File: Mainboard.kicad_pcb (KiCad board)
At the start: 4 copper layers, 100 x 60 mm, 137 parts, among them J1 USB_B_Micro, J10 Conn_01x02_Male, J11 Conn_01x02_Male, J12 Conn_01x02_Male, J2 8P8C_LED, J3 Micro_SD_Card_Det, J4 Conn_Coaxial, J5 Conn_Coaxial, J6 Screw_Terminal_01x02, J7 Screw_Terminal_01x02, J8 Screw_Terminal_01x02, J9 Conn_01x02_Male, Q1 MMDT2222A, Q3 PMV20ENR, Q4 PMV20ENR, Q5 PMV20ENR, U1 CP2102N-A01-GQFN24, U10 LTV-817S, U11 RFM95W-868S2, U2 SN65HVD230, U3 ESP32-WROOM-32D, U4 W25Q64FV, U5 MS5607-02BA, U6 MAX-M8Q, U7 LSM9DS1, U8 TPS63031, U9 LTV-817S

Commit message: routed almost all 3.3
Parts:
- removed REF** (x4): MountingHole_3.2mm_M3_DIN965_Pad, MountingHole:MountingHole_3.2mm_M3_DIN965_Pad
- added H1: MountingHole_Pad, MountingHole:MountingHole_3.2mm_M3_DIN965_Pad, F.Cu at (88.1, 53.1)
- added H2: MountingHole_Pad, MountingHole:MountingHole_3.2mm_M3_DIN965_Pad, F.Cu at (88.0, 107.0)
- added H3: MountingHole_Pad, MountingHole:MountingHole_3.2mm_M3_DIN965_Pad, F.Cu at (181.9, 53.0)
- added H4: MountingHole_Pad, MountingHole:MountingHole_3.2mm_M3_DIN965_Pad, F.Cu at (182.0, 107.0)
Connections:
- U3 pad 39: (no net) -> GND
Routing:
- net +3V3: track 90.6 -> 134.3 mm, vias 0 -> 16
- net GND: track 25.1 -> 27.9 mm
- added copper zone on In1.Cu, net +3V3

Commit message: update
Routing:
- net +3V3: track 134.3 -> 156.0 mm, vias 16 -> 18
- net VDD: track 17.0 -> 24.8 mm
- net GND: track 27.9 -> 30.0 mm, vias 0 -> 9

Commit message: update
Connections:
- U3 pad 8: /CAN_RX -> /CAN_TX
- U3 pad 9: /CAN_TX -> /CAN_RX
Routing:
- net /CAN_RX: track 50.0 -> 73.8 mm
- net /CAN_TX: track 67.1 -> 44.3 mm
- net GND: track 30.0 -> 43.3 mm, vias 9 -> 11
- net /LORA_CS: track 85.0 -> 91.6 mm
- net /Nuke1: track 88.9 -> 82.2 mm
- net /BOOT: track 82.7 -> 76.6 mm
- net /LORA_RESET: track 89.2 -> 83.4 mm
- net /SCL: track 112.1 -> 108.7 mm
- net /Buzzer: track 82.0 -> 84.9 mm
- net /CAN_HIGH: track 28.5 -> 26.3 mm
- net /SDA: track 104.8 -> 103.0 mm
- net /DTR: track 37.9 -> 36.3 mm
- net /FLASH_CS: track 88.2 -> 89.7 mm
- net /RADIO_RX: track 38.3 -> 39.8 mm
- net /RADIO_TX: track 37.8 -> 39.2 mm
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- removed copper zone on In1.Cu, net +3V3

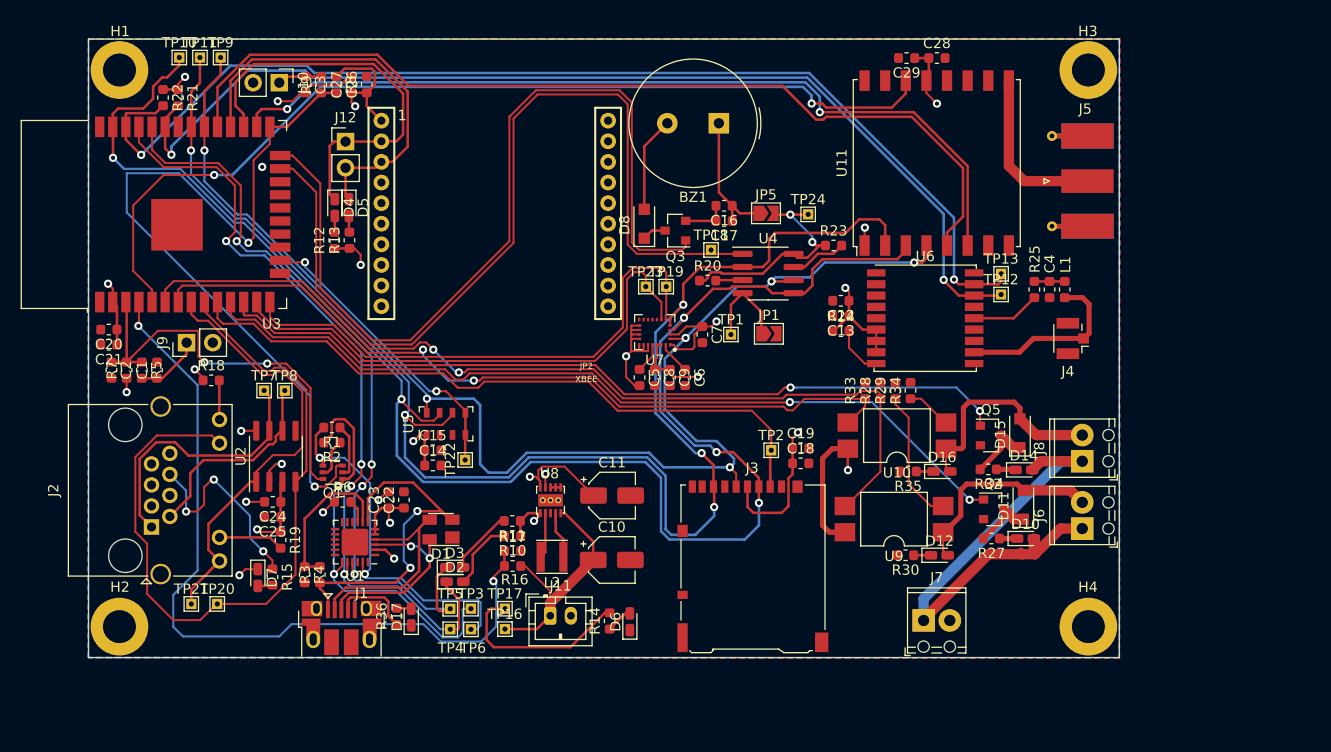
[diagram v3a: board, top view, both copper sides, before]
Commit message: replaced screw terminals with ramps connectors
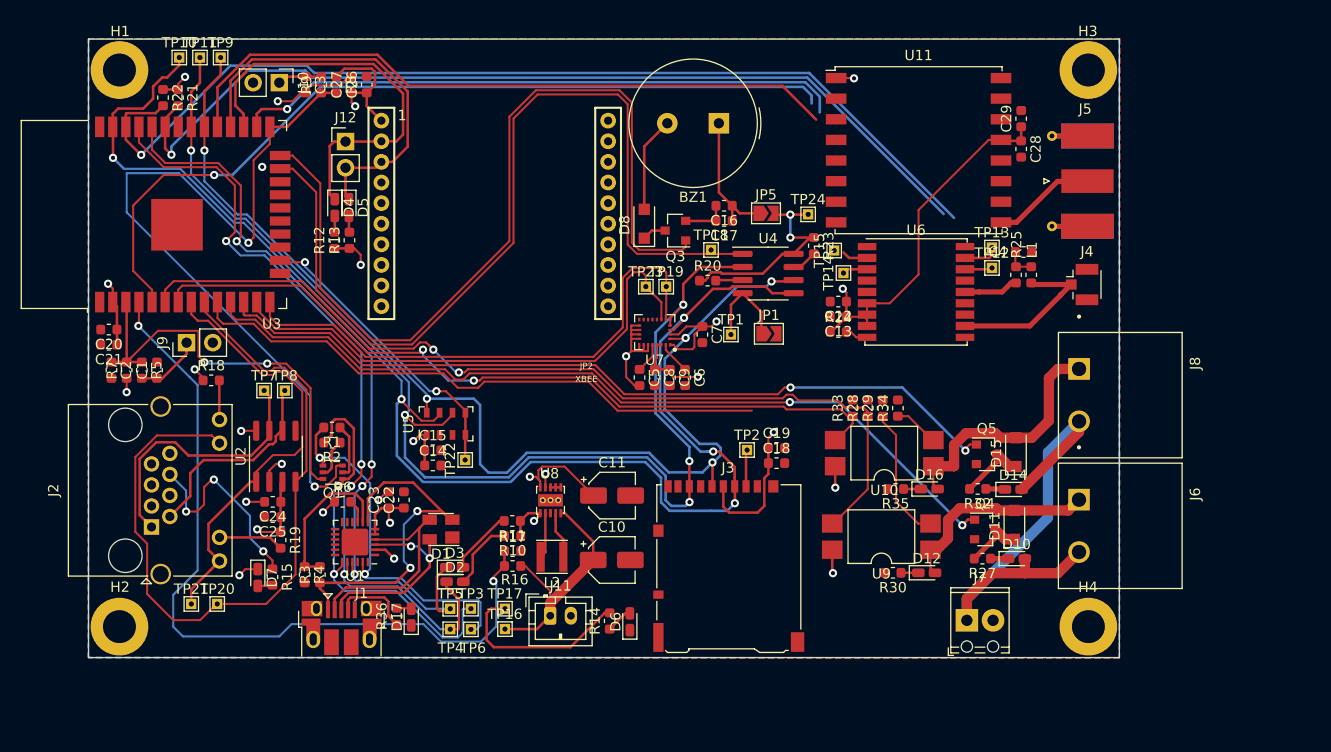
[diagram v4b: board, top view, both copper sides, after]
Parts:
- added TP14: TestPoint, TestPoint:TestPoint_THTPad_1.0x1.0mm_Drill0.5mm, F.Cu at (158.2, 72.7)
- added TP15: TestPoint, TestPoint:TestPoint_THTPad_1.0x1.0mm_Drill0.5mm, F.Cu at (157.3, 70.5)
- J6, J8: footprint TerminalBlock_Phoenix:TerminalBlock_Phoenix_MPT-0,5-2-2.54_1x02_P2.54mm_Horizontal -> iclr-hw:PHOENIX_1757242
- moved C29 12.6 mm to (175.5, 57.7), turned to 90 degrees
- moved C28 12.0 mm to (175.5, 60.7), turned to 270 degrees
- moved J8 7.40 mm to (185.1, 84.5), turned to 270 degrees
- moved J4 5.31 mm to (181.4, 73.8), turned to 0 degrees
- moved C4 4.43 mm to (175.7, 70.7), turned to 0 degrees
- moved J7 4.20 mm to (170.2, 106.4)
- moved J6 3.69 mm to (185.1, 97.2), turned to 270 degrees
- moved L1 3.55 mm to (176.5, 72.9)
- moved TP12 2.72 mm to (172.6, 72.2)
- moved TP13 2.70 mm to (172.6, 70.2)
- moved U6 2.70 mm to (165.3, 74.5)
- moved C18 2.34 mm to (151.7, 91.1)
- moved C19 2.34 mm to (151.7, 89.7)
- moved J3 2.34 mm to (147.1, 101.1)
- moved TP2 2.34 mm to (148.9, 89.9)
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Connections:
- J6 pad 1: /nukes/External_Supply -> Net-(D11-Pad2)
- J6 pad 2: Net-(D11-Pad2) -> /nukes/External_Supply
- J8 pad 1: /nukes/External_Supply -> Net-(D15-Pad2)
- J8 pad 2: Net-(D15-Pad2) -> /nukes/External_Supply
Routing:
- net /MISO: track 147.5 -> 119.8 mm
- net /LORA_CS: track 91.6 -> 67.1 mm
- net /LORA_RESET: track 83.4 -> 59.2 mm, vias 2 -> 1
- net /MOSI: track 162.3 -> 139.5 mm
- net /SCLK: track 132.9 -> 113.9 mm, vias 6 -> 5
- net /LORA_INT: track 93.5 -> 82.3 mm, vias 2 -> 1
- net +3V3: track 156.0 -> 166.7 mm
- net /SDA: track 103.0 -> 93.0 mm, vias 2 -> 1
- net /SCL: track 108.7 -> 100.6 mm, vias 2 -> 1
- net Net-(J5-Pad1): track 16.5 -> 10.0 mm
- net /SD_CS: track 69.8 -> 65.2 mm
- net Net-(R23-Pad2): track 5.53 -> 2.49 mm
- net Net-(D15-Pad2): track 21.6 -> 24.4 mm
- net Net-(R24-Pad2): track 4.89 -> 2.24 mm
- net /GPS/TXD: track 0.00 -> 2.51 mm
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
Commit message: udpate
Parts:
- added REF**: VIA-0.6mm, iclr-hw:VIA-0.6mm, F.Cu at (183.5, 77.8)
- added REF**: VIA-0.6mm, iclr-hw:VIA-0.6mm, F.Cu at (167.7, 72.6)
- added REF**: VIA-0.6mm, iclr-hw:VIA-0.6mm, F.Cu at (162.5, 72.6)
- added REF**: VIA-0.6mm, iclr-hw:VIA-0.6mm, F.Cu at (157.2, 72.6)
- added REF**: VIA-0.6mm, iclr-hw:VIA-0.6mm, F.Cu at (183.5, 67.3)
- added REF**: VIA-0.6mm, iclr-hw:VIA-0.6mm, F.Cu at (178.2, 67.3)
- added REF**: VIA-0.6mm, iclr-hw:VIA-0.6mm, F.Cu at (173.0, 67.3)
- added REF**: VIA-0.6mm, iclr-hw:VIA-0.6mm, F.Cu at (167.7, 67.3)
- added REF**: VIA-0.6mm, iclr-hw:VIA-0.6mm, F.Cu at (162.5, 67.3)
- added REF**: VIA-0.6mm, iclr-hw:VIA-0.6mm, F.Cu at (157.2, 67.3)
- added REF**: VIA-0.6mm, iclr-hw:VIA-0.6mm, F.Cu at (183.5, 62.1)
- added REF**: VIA-0.6mm, iclr-hw:VIA-0.6mm, F.Cu at (178.2, 77.8)
- added REF**: VIA-0.6mm, iclr-hw:VIA-0.6mm, F.Cu at (178.2, 62.1)
- added REF**: VIA-0.6mm, iclr-hw:VIA-0.6mm, F.Cu at (173.0, 62.1)
- added REF**: VIA-0.6mm, iclr-hw:VIA-0.6mm, F.Cu at (167.7, 62.1)
- added REF**: VIA-0.6mm, iclr-hw:VIA-0.6mm, F.Cu at (162.5, 62.1)
- added REF**: VIA-0.6mm, iclr-hw:VIA-0.6mm, F.Cu at (157.2, 62.1)
- added REF**: VIA-0.6mm, iclr-hw:VIA-0.6mm, F.Cu at (183.5, 56.8)
- added REF**: VIA-0.6mm, iclr-hw:VIA-0.6mm, F.Cu at (178.2, 56.8)
- added REF**: VIA-0.6mm, iclr-hw:VIA-0.6mm, F.Cu at (173.0, 56.8)
- added REF**: VIA-0.6mm, iclr-hw:VIA-0.6mm, F.Cu at (167.7, 56.8)
- added REF**: VIA-0.6mm, iclr-hw:VIA-0.6mm, F.Cu at (162.5, 56.8)
- added REF**: VIA-0.6mm, iclr-hw:VIA-0.6mm, F.Cu at (173.0, 77.8)
- added REF**: VIA-0.6mm, iclr-hw:VIA-0.6mm, F.Cu at (157.2, 56.8)
- added REF**: VIA-0.6mm, iclr-hw:VIA-0.6mm, F.Cu at (178.2, 51.6)
- added REF**: VIA-0.6mm, iclr-hw:VIA-0.6mm, F.Cu at (173.0, 51.6)
- added REF**: VIA-0.6mm, iclr-hw:VIA-0.6mm, F.Cu at (167.7, 51.6)
- added REF**: VIA-0.6mm, iclr-hw:VIA-0.6mm, F.Cu at (162.5, 51.6)
- added REF**: VIA-0.6mm, iclr-hw:VIA-0.6mm, F.Cu at (157.2, 51.6)
- added REF**: VIA-0.6mm, iclr-hw:VIA-0.6mm, F.Cu at (167.7, 77.8)
- added REF**: VIA-0.6mm, iclr-hw:VIA-0.6mm, F.Cu at (162.5, 77.8)
- added REF**: VIA-0.6mm, iclr-hw:VIA-0.6mm, F.Cu at (157.2, 77.8)
- added REF**: VIA-0.6mm, iclr-hw:VIA-0.6mm, F.Cu at (183.5, 72.6)
- added REF**: VIA-0.6mm, iclr-hw:VIA-0.6mm, F.Cu at (178.2, 72.6)
- added REF**: VIA-0.6mm, iclr-hw:VIA-0.6mm, F.Cu at (173.0, 72.6)
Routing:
- net /LORA_INT: track 82.3 -> 107.1 mm, vias 1 -> 2
- net /MISO: track 119.8 -> 142.4 mm, vias 5 -> 7
- net /MOSI: track 139.5 -> 161.4 mm, vias 5 -> 7
- net /SCLK: track 113.9 -> 133.6 mm, vias 5 -> 6
- net /LORA_RESET: track 59.2 -> 75.0 mm, vias 1 -> 2
- net +3V3: track 166.7 -> 179.2 mm, vias 18 -> 17
- net /SDA: track 93.0 -> 104.3 mm, vias 1 -> 2
- net /SCL: track 100.6 -> 109.8 mm, vias 1 -> 2
- net /LORA_CS: track 67.1 -> 74.0 mm
- net GND: track 43.0 -> 41.3 mm, vias 11 -> 10
- added copper zone on In1.Cu, net +3V3
- added copper zone on In1.Cu, net GND

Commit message: shroom
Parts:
- removed the REF** at (183.5, 77.8)
- removed the REF** at (167.7, 72.6)
- removed the REF** at (162.5, 72.6)
- removed the REF** at (157.2, 72.6)
- removed the REF** at (183.5, 67.3)
- removed the REF** at (178.2, 67.3)
- removed the REF** at (173.0, 67.3)
- removed the REF** at (167.7, 67.3)
- removed the REF** at (162.5, 67.3)
- removed the REF** at (157.2, 67.3)
- removed the REF** at (183.5, 62.1)
- removed the REF** at (178.2, 77.8)
- removed the REF** at (178.2, 62.1)
- removed the REF** at (173.0, 62.1)
- removed the REF** at (167.7, 62.1)
- removed the REF** at (162.5, 62.1)
- removed the REF** at (157.2, 62.1)
- removed the REF** at (183.5, 56.8)
- removed the REF** at (178.2, 56.8)
- removed the REF** at (173.0, 56.8)
- removed the REF** at (167.7, 56.8)
- removed the REF** at (162.5, 56.8)
- removed the REF** at (173.0, 77.8)
- removed the REF** at (157.2, 56.8)
- removed the REF** at (178.2, 51.6)
- removed the REF** at (173.0, 51.6)
- removed the REF** at (167.7, 51.6)
- removed the REF** at (162.5, 51.6)
- removed the REF** at (157.2, 51.6)
- removed the REF** at (167.7, 77.8)
- removed the REF** at (162.5, 77.8)
- removed the REF** at (157.2, 77.8)
- removed the REF** at (183.5, 72.6)
- removed the REF** at (178.2, 72.6)
- removed the REF** at (173.0, 72.6)
- added REF**: SolderJumper-3_P1.3mm_Bridged2Bar12_RoundedPad1.0x1.5mm_Num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, Jumper:SolderJumper-3_P1.3mm_Bridged2Bar12_RoundedPad1.0x1.5mm_NumberLabels, F.Cu at (102.9, 81.8)
- added REF**: VIA-0.6mm, iclr-hw:VIA-0.6mm, F.Cu at (176.8, 66.5)
- added REF**: VIA-0.6mm, iclr-hw:VIA-0.6mm, F.Cu at (176.1, 67.2)
- added REF**: VIA-0.6mm, iclr-hw:VIA-0.6mm, F.Cu at (175.4, 67.9)
- added REF**: VIA-0.6mm, iclr-hw:VIA-0.6mm, F.Cu at (174.6, 68.5)
- added REF**: VIA-0.6mm, iclr-hw:VIA-0.6mm, F.Cu at (177.7, 70.1)
- added REF**: VIA-0.6mm, iclr-hw:VIA-0.6mm, F.Cu at (177.7, 72.1)
- added REF**: VIA-0.6mm, iclr-hw:VIA-0.6mm, F.Cu at (177.7, 71.1)
- added REF**: VIA-0.6mm, iclr-hw:VIA-0.6mm, F.Cu at (178.2, 69.7)
- added REF**: VIA-0.6mm, iclr-hw:VIA-0.6mm, F.Cu at (176.5, 68.3)
- added REF**: VIA-0.6mm, iclr-hw:VIA-0.6mm, F.Cu at (176.2, 69.7)
- added REF**: SolderJumper-3_P1.3mm_Bridged2Bar12_RoundedPad1.0x1.5mm_Num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, Jumper:SolderJumper-3_P1.3mm_Bridged2Bar12_RoundedPad1.0x1.5mm_NumberLabels, F.Cu at (100.4, 81.8)
- added REF**: VIA-0.6mm, iclr-hw:VIA-0.6mm, F.Cu at (175.2, 69.7)
- added REF**: VIA-0.6mm, iclr-hw:VIA-0.6mm, F.Cu at (174.2, 69.7)
- added REF**: VIA-0.6mm, iclr-hw:VIA-0.6mm, F.Cu at (174.0, 70.8)
- added REF**: VIA-0.6mm, iclr-hw:VIA-0.6mm, F.Cu at (174.0, 71.8)
- added REF**: VIA-0.6mm, iclr-hw:VIA-0.6mm, F.Cu at (174.0, 72.8)
- added REF**: VIA-0.6mm, iclr-hw:VIA-0.6mm, F.Cu at (173.8, 73.8)
- added REF**: VIA-0.6mm, iclr-hw:VIA-0.6mm, F.Cu at (172.8, 73.8)
- added REF**: VIA-0.6mm, iclr-hw:VIA-0.6mm, F.Cu at (171.8, 73.8)
- added REF**: VIA-0.6mm, iclr-hw:VIA-0.6mm, F.Cu at (175.6, 74.7)
- added REF**: VIA-0.6mm, iclr-hw:VIA-0.6mm, F.Cu at (174.8, 75.2)
- added REF**: VIA-0.6mm, iclr-hw:VIA-0.6mm, F.Cu at (177.9, 63.3)
- added REF**: VIA-0.6mm, iclr-hw:VIA-0.6mm, F.Cu at (173.8, 75.2)
- added REF**: VIA-0.6mm, iclr-hw:VIA-0.6mm, F.Cu at (172.8, 75.2)
- added REF**: VIA-0.6mm, iclr-hw:VIA-0.6mm, F.Cu at (171.8, 75.2)
- added REF**: VIA-0.6mm, iclr-hw:VIA-0.6mm, F.Cu at (176.6, 74.6)
- added REF**: VIA-0.6mm, iclr-hw:VIA-0.6mm, F.Cu at (178.6, 74.5)
- added REF**: VIA-0.6mm, iclr-hw:VIA-0.6mm, F.Cu at (177.6, 74.5)
- added REF**: VIA-0.6mm, iclr-hw:VIA-0.6mm, F.Cu at (177.4, 73.1)
- added REF**: VIA-0.6mm, iclr-hw:VIA-0.6mm, F.Cu at (179.4, 73.1)
- added REF**: VIA-0.6mm, iclr-hw:VIA-0.6mm, F.Cu at (180.3, 72.8)
- added REF**: VIA-0.6mm, iclr-hw:VIA-0.6mm, F.Cu at (177.9, 75.2)
- added REF**: VIA-0.6mm, iclr-hw:VIA-0.6mm, F.Cu at (177.2, 64.0)
- added REF**: VIA-0.6mm, iclr-hw:VIA-0.6mm, F.Cu at (177.2, 75.9)
- added REF**: VIA-0.6mm, iclr-hw:VIA-0.6mm, F.Cu at (176.5, 76.6)
- added REF**: VIA-0.6mm, iclr-hw:VIA-0.6mm, F.Cu at (176.9, 76.8)
- added REF**: VIA-0.6mm, iclr-hw:VIA-0.6mm, F.Cu at (175.9, 76.8)
- added REF**: VIA-0.6mm, iclr-hw:VIA-0.6mm, F.Cu at (174.9, 76.8)
- added REF**: VIA-0.6mm, iclr-hw:VIA-0.6mm, F.Cu at (173.9, 76.8)
- added REF**: VIA-0.6mm, iclr-hw:VIA-0.6mm, F.Cu at (172.9, 76.8)
- added REF**: VIA-0.6mm, iclr-hw:VIA-0.6mm, F.Cu at (176.9, 78.3)
- added REF**: VIA-0.6mm, iclr-hw:VIA-0.6mm, F.Cu at (175.9, 78.3)
- added REF**: VIA-0.6mm, iclr-hw:VIA-0.6mm, F.Cu at (180.2, 74.9)
- added REF**: VIA-0.6mm, iclr-hw:VIA-0.6mm, F.Cu at (176.5, 64.7)
- added REF**: VIA-0.6mm, iclr-hw:VIA-0.6mm, F.Cu at (179.2, 76.0)
- added REF**: VIA-0.6mm, iclr-hw:VIA-0.6mm, F.Cu at (178.8, 76.3)
- added REF**: VIA-0.6mm, iclr-hw:VIA-0.6mm, F.Cu at (178.1, 77.1)
- added REF**: VIA-0.6mm, iclr-hw:VIA-0.6mm, F.Cu at (177.9, 78.3)
- added REF**: VIA-0.6mm, iclr-hw:VIA-0.6mm, F.Cu at (174.9, 78.3)
- added REF**: VIA-0.6mm, iclr-hw:VIA-0.6mm, F.Cu at (173.9, 78.3)
- added REF**: VIA-0.6mm, iclr-hw:VIA-0.6mm, F.Cu at (183.5, 78.3)
- added REF**: VIA-0.6mm, iclr-hw:VIA-0.6mm, F.Cu at (177.4, 77.8)
- added REF**: VIA-0.6mm, iclr-hw:VIA-0.6mm, F.Cu at (172.9, 78.3)
- added REF**: VIA-0.6mm, iclr-hw:VIA-0.6mm, F.Cu at (167.6, 78.3)
- added REF**: VIA-0.6mm, iclr-hw:VIA-0.6mm, F.Cu at (175.8, 65.4)
- added REF**: VIA-0.6mm, iclr-hw:VIA-0.6mm, F.Cu at (162.3, 78.3)
- added REF**: VIA-0.6mm, iclr-hw:VIA-0.6mm, F.Cu at (183.5, 73.0)
- added REF**: VIA-0.6mm, iclr-hw:VIA-0.6mm, F.Cu at (178.4, 73.1)
- added REF**: VIA-0.6mm, iclr-hw:VIA-0.6mm, F.Cu at (167.6, 73.0)
- added REF**: VIA-0.6mm, iclr-hw:VIA-0.6mm, F.Cu at (162.3, 73.0)
- added REF**: VIA-0.6mm, iclr-hw:VIA-0.6mm, F.Cu at (157.0, 73.0)
- added REF**: VIA-0.6mm, iclr-hw:VIA-0.6mm, F.Cu at (183.5, 67.7)
- added REF**: VIA-0.6mm, iclr-hw:VIA-0.6mm, F.Cu at (178.2, 67.7)
- added REF**: VIA-0.6mm, iclr-hw:VIA-0.6mm, F.Cu at (172.9, 67.7)
- added REF**: VIA-0.6mm, iclr-hw:VIA-0.6mm, F.Cu at (167.6, 67.7)
- added REF**: VIA-0.6mm, iclr-hw:VIA-0.6mm, F.Cu at (175.1, 66.1)
- added REF**: VIA-0.6mm, iclr-hw:VIA-0.6mm, F.Cu at (162.3, 67.7)
- added REF**: VIA-0.6mm, iclr-hw:VIA-0.6mm, F.Cu at (157.0, 67.7)
- added REF**: VIA-0.6mm, iclr-hw:VIA-0.6mm, F.Cu at (183.5, 62.4)
- added REF**: VIA-0.6mm, iclr-hw:VIA-0.6mm, F.Cu at (178.2, 62.4)
- added REF**: VIA-0.6mm, iclr-hw:VIA-0.6mm, F.Cu at (172.9, 62.4)
- added REF**: VIA-0.6mm, iclr-hw:VIA-0.6mm, F.Cu at (167.6, 62.4)
- added REF**: VIA-0.6mm, iclr-hw:VIA-0.6mm, F.Cu at (162.3, 62.4)
- added REF**: VIA-0.6mm, iclr-hw:VIA-0.6mm, F.Cu at (157.0, 62.4)
- added REF**: VIA-0.6mm, iclr-hw:VIA-0.6mm, F.Cu at (183.5, 57.1)
- added REF**: VIA-0.6mm, iclr-hw:VIA-0.6mm, F.Cu at (178.2, 57.1)
- added REF**: VIA-0.6mm, iclr-hw:VIA-0.6mm, F.Cu at (174.4, 66.8)
- added REF**: VIA-0.6mm, iclr-hw:VIA-0.6mm, F.Cu at (172.9, 57.1)
- added REF**: VIA-0.6mm, iclr-hw:VIA-0.6mm, F.Cu at (167.6, 57.1)
- added REF**: VIA-0.6mm, iclr-hw:VIA-0.6mm, F.Cu at (162.3, 57.1)
- added REF**: VIA-0.6mm, iclr-hw:VIA-0.6mm, F.Cu at (157.0, 57.1)
- added REF**: VIA-0.6mm, iclr-hw:VIA-0.6mm, F.Cu at (178.2, 51.8)
- added REF**: VIA-0.6mm, iclr-hw:VIA-0.6mm, F.Cu at (172.9, 51.8)
- added REF**: VIA-0.6mm, iclr-hw:VIA-0.6mm, F.Cu at (167.6, 51.8)
- added REF**: VIA-0.6mm, iclr-hw:VIA-0.6mm, F.Cu at (162.3, 51.8)
- added REF**: VIA-0.6mm, iclr-hw:VIA-0.6mm, F.Cu at (157.0, 51.8)
- added REF**: VIA-0.6mm, iclr-hw:VIA-0.6mm, F.Cu at (178.2, 65.0)
- J7: footprint TerminalBlock_Phoenix:TerminalBlock_Phoenix_MPT-0,5-2-2.54_1x02_P2.54mm_Horizontal -> iclr-hw:PHOENIX_1757242
- U1: footprint Package_DFN_QFN:QFN-24-1EP_4x4mm_P0.5mm_EP2.6x2.6mm -> Package_DFN_QFN:QFN-24-1EP_4x4mm_P0.5mm_EP2.6x2.6mm_ThermalVias
- moved J7 3.16 mm to (168.1, 108.8), turned to 180 degrees
- moved D10 2.99 mm to (175.2, 97.4)
- moved D11 2.99 mm to (175.0, 94.1)
- moved D16 2.99 mm to (166.7, 90.7)
- moved Q5 2.99 mm to (172.3, 87.3)
- moved R28 2.99 mm to (160.8, 82.8)
- moved R30 2.99 mm to (163.2, 98.8)
- moved R33 2.99 mm to (159.3, 82.8)
- moved U10 2.99 mm to (162.4, 87.2)
- moved D12 2.99 mm to (166.5, 98.8)
- moved Q4 2.99 mm to (172.1, 94.6)
- moved R27 2.99 mm to (171.9, 97.4)
- moved R34 2.99 mm to (163.7, 82.8)
- moved R35 2.99 mm to (163.5, 90.7)
- moved U9 2.99 mm to (162.1, 95.3)
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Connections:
- J7 pad 1: /nukes/External_Supply -> GND
- J7 pad 2: GND -> /nukes/External_Supply
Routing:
- net /EN: track 41.2 -> 48.0 mm
- net /CAN_LOW: track 19.9 -> 26.0 mm, vias 0 -> 1
- net /CAN_HIGH: track 26.3 -> 32.4 mm
- net GND: track 41.3 -> 46.1 mm
- net /BOOT: track 76.6 -> 81.3 mm
- net /nukes/External_Supply: track 49.0 -> 53.0 mm
- net +3V3: track 179.2 -> 183.1 mm, vias 17 -> 15
- net Net-(D15-Pad2): track 24.4 -> 20.6 mm
- net /CAN_TX: track 44.3 -> 47.0 mm
- net /TXD: track 75.5 -> 77.5 mm
- net /CAN_RX: track 73.8 -> 75.6 mm
- net /RXD: track 78.2 -> 79.7 mm
- net /Cont2: track 76.0 -> 77.3 mm
- net /SD_CS: track 65.2 -> 66.5 mm
- net /RTS: track 40.3 -> 41.6 mm
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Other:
- net class rf1 added: clearance 0.2, trace_width 0.33559, via_dia 0.8, via_drill 0.4

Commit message: stiched
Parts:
- added J3: Micro_SD_Card_Det, Connector_Card:microSD_HC_Hirose_DM3AT-SF-PEJM5, F.Cu at (147.1, 98.4)
- added REF**: VIA-0.6mm, iclr-hw:VIA-0.6mm, F.Cu at (184.5, 101.8)
- added REF**: VIA-0.6mm, iclr-hw:VIA-0.6mm, F.Cu at (184.5, 81.5)
- added REF**: VIA-0.6mm, iclr-hw:VIA-0.6mm, F.Cu at (85.5, 96.2)
- added REF**: VIA-0.6mm, iclr-hw:VIA-0.6mm, F.Cu at (85.5, 83.5)
- added REF**: VIA-0.6mm, iclr-hw:VIA-0.6mm, F.Cu at (85.5, 81.0)
- added REF**: VIA-0.6mm, iclr-hw:VIA-0.6mm, F.Cu at (85.5, 103.9)
- added REF**: VIA-0.6mm, iclr-hw:VIA-0.6mm, F.Cu at (85.5, 101.3)
- added REF**: VIA-0.6mm, iclr-hw:VIA-0.6mm, F.Cu at (85.5, 98.8)
- added REF**: VIA-0.6mm, iclr-hw:VIA-0.6mm, F.Cu at (85.5, 93.7)
- added REF**: VIA-0.6mm, iclr-hw:VIA-0.6mm, F.Cu at (85.5, 91.2)
- added REF**: VIA-0.6mm, iclr-hw:VIA-0.6mm, F.Cu at (85.5, 88.6)
- added REF**: VIA-0.6mm, iclr-hw:VIA-0.6mm, F.Cu at (184.5, 89.2)
- added REF**: VIA-0.6mm, iclr-hw:VIA-0.6mm, F.Cu at (85.5, 86.1)
- added REF**: VIA-0.6mm, iclr-hw:VIA-0.6mm, F.Cu at (85.5, 73.4)
- added REF**: VIA-0.6mm, iclr-hw:VIA-0.6mm, F.Cu at (85.5, 70.8)
- added REF**: VIA-0.6mm, iclr-hw:VIA-0.6mm, F.Cu at (85.5, 68.3)
- added REF**: VIA-0.6mm, iclr-hw:VIA-0.6mm, F.Cu at (85.5, 65.8)
- added REF**: VIA-0.6mm, iclr-hw:VIA-0.6mm, F.Cu at (85.5, 63.2)
- added REF**: VIA-0.6mm, iclr-hw:VIA-0.6mm, F.Cu at (85.5, 60.7)
- added REF**: VIA-0.6mm, iclr-hw:VIA-0.6mm, F.Cu at (85.5, 55.6)
- added REF**: VIA-0.6mm, iclr-hw:VIA-0.6mm, F.Cu at (131.2, 109.5)
- added REF**: VIA-0.6mm, iclr-hw:VIA-0.6mm, F.Cu at (118.5, 109.5)
- added REF**: VIA-0.6mm, iclr-hw:VIA-0.6mm, F.Cu at (184.5, 86.6)
- added REF**: VIA-0.6mm, iclr-hw:VIA-0.6mm, F.Cu at (116.0, 109.5)
- added REF**: VIA-0.6mm, iclr-hw:VIA-0.6mm, F.Cu at (113.5, 109.5)
- added REF**: VIA-0.6mm, iclr-hw:VIA-0.6mm, F.Cu at (177.0, 109.5)
- added REF**: VIA-0.6mm, iclr-hw:VIA-0.6mm, F.Cu at (174.4, 109.5)
- added REF**: VIA-0.6mm, iclr-hw:VIA-0.6mm, F.Cu at (171.9, 109.5)
- added REF**: VIA-0.6mm, iclr-hw:VIA-0.6mm, F.Cu at (169.3, 109.5)
- added REF**: VIA-0.6mm, iclr-hw:VIA-0.6mm, F.Cu at (166.8, 109.5)
- added REF**: VIA-0.6mm, iclr-hw:VIA-0.6mm, F.Cu at (164.3, 109.5)
- added REF**: VIA-0.6mm, iclr-hw:VIA-0.6mm, F.Cu at (161.7, 109.5)
- added REF**: VIA-0.6mm, iclr-hw:VIA-0.6mm, F.Cu at (159.2, 109.5)
- added REF**: VIA-0.6mm, iclr-hw:VIA-0.6mm, F.Cu at (184.5, 84.1)
- added REF**: VIA-0.6mm, iclr-hw:VIA-0.6mm, F.Cu at (156.7, 109.5)
- added REF**: VIA-0.6mm, iclr-hw:VIA-0.6mm, F.Cu at (151.6, 109.5)
- added REF**: VIA-0.6mm, iclr-hw:VIA-0.6mm, F.Cu at (149.0, 109.5)
- added REF**: VIA-0.6mm, iclr-hw:VIA-0.6mm, F.Cu at (146.5, 109.5)
- added REF**: VIA-0.6mm, iclr-hw:VIA-0.6mm, F.Cu at (143.9, 109.5)
- added REF**: VIA-0.6mm, iclr-hw:VIA-0.6mm, F.Cu at (141.4, 109.5)
- added REF**: VIA-0.6mm, iclr-hw:VIA-0.6mm, F.Cu at (138.9, 109.5)
- added REF**: VIA-0.6mm, iclr-hw:VIA-0.6mm, F.Cu at (136.3, 109.5)
- added REF**: VIA-0.6mm, iclr-hw:VIA-0.6mm, F.Cu at (133.8, 109.5)
- added REF**: VIA-0.6mm, iclr-hw:VIA-0.6mm, F.Cu at (128.7, 109.5)
- added REF**: VIA-0.6mm, iclr-hw:VIA-0.6mm, F.Cu at (184.5, 104.4)
- added REF**: VIA-0.6mm, iclr-hw:VIA-0.6mm, F.Cu at (126.2, 109.5)
- added REF**: VIA-0.6mm, iclr-hw:VIA-0.6mm, F.Cu at (123.6, 109.5)
- added REF**: VIA-0.6mm, iclr-hw:VIA-0.6mm, F.Cu at (121.1, 109.5)
- added REF**: VIA-0.6mm, iclr-hw:VIA-0.6mm, F.Cu at (110.9, 109.5)
- added REF**: VIA-0.6mm, iclr-hw:VIA-0.6mm, F.Cu at (108.4, 109.5)
- added REF**: VIA-0.6mm, iclr-hw:VIA-0.6mm, F.Cu at (105.8, 109.5)
- added REF**: VIA-0.6mm, iclr-hw:VIA-0.6mm, F.Cu at (103.3, 109.5)
- added REF**: VIA-0.6mm, iclr-hw:VIA-0.6mm, F.Cu at (100.8, 109.5)
- added REF**: VIA-0.6mm, iclr-hw:VIA-0.6mm, F.Cu at (98.2, 109.5)
- added REF**: VIA-0.6mm, iclr-hw:VIA-0.6mm, F.Cu at (95.7, 109.5)
- added REF**: VIA-0.6mm, iclr-hw:VIA-0.6mm, F.Cu at (184.5, 99.3)
- added REF**: VIA-0.6mm, iclr-hw:VIA-0.6mm, F.Cu at (93.2, 109.5)
- added REF**: VIA-0.6mm, iclr-hw:VIA-0.6mm, F.Cu at (91.0, 50.5)
- added REF**: VIA-0.6mm, iclr-hw:VIA-0.6mm, F.Cu at (136.8, 50.5)
- added REF**: VIA-0.6mm, iclr-hw:VIA-0.6mm, F.Cu at (124.1, 50.5)
- added REF**: VIA-0.6mm, iclr-hw:VIA-0.6mm, F.Cu at (121.5, 50.5)
- added REF**: VIA-0.6mm, iclr-hw:VIA-0.6mm, F.Cu at (119.0, 50.5)
- added REF**: VIA-0.6mm, iclr-hw:VIA-0.6mm, F.Cu at (154.6, 50.5)
- added REF**: VIA-0.6mm, iclr-hw:VIA-0.6mm, F.Cu at (152.0, 50.5)
- added REF**: VIA-0.6mm, iclr-hw:VIA-0.6mm, F.Cu at (149.5, 50.5)
- added REF**: VIA-0.6mm, iclr-hw:VIA-0.6mm, F.Cu at (146.9, 50.5)
- added REF**: VIA-0.6mm, iclr-hw:VIA-0.6mm, F.Cu at (184.5, 96.8)
- added REF**: VIA-0.6mm, iclr-hw:VIA-0.6mm, F.Cu at (144.4, 50.5)
- added REF**: VIA-0.6mm, iclr-hw:VIA-0.6mm, F.Cu at (141.8, 50.5)
- added REF**: VIA-0.6mm, iclr-hw:VIA-0.6mm, F.Cu at (139.3, 50.5)
- added REF**: VIA-0.6mm, iclr-hw:VIA-0.6mm, F.Cu at (134.2, 50.5)
- added REF**: VIA-0.6mm, iclr-hw:VIA-0.6mm, F.Cu at (131.7, 50.5)
- added REF**: VIA-0.6mm, iclr-hw:VIA-0.6mm, F.Cu at (129.2, 50.5)
- added REF**: VIA-0.6mm, iclr-hw:VIA-0.6mm, F.Cu at (126.6, 50.5)
- added REF**: VIA-0.6mm, iclr-hw:VIA-0.6mm, F.Cu at (116.5, 50.5)
- added REF**: VIA-0.6mm, iclr-hw:VIA-0.6mm, F.Cu at (113.9, 50.5)
- added REF**: VIA-0.6mm, iclr-hw:VIA-0.6mm, F.Cu at (111.4, 50.5)
- added REF**: VIA-0.6mm, iclr-hw:VIA-0.6mm, F.Cu at (184.5, 94.2)
- added REF**: VIA-0.6mm, iclr-hw:VIA-0.6mm, F.Cu at (108.8, 50.5)
- added REF**: VIA-0.6mm, iclr-hw:VIA-0.6mm, F.Cu at (106.3, 50.5)
- added REF**: VIA-0.6mm, iclr-hw:VIA-0.6mm, F.Cu at (103.8, 50.5)
- added REF**: VIA-0.6mm, iclr-hw:VIA-0.6mm, F.Cu at (101.2, 50.5)
- added REF**: VIA-0.6mm, iclr-hw:VIA-0.6mm, F.Cu at (93.6, 50.5)
- added REF**: VIA-0.6mm, iclr-hw:VIA-0.6mm, F.Cu at (96.1, 50.5)
- added REF**: VIA-0.6mm, iclr-hw:VIA-0.6mm, F.Cu at (98.7, 50.5)
- added REF**: VIA-0.6mm, iclr-hw:VIA-0.6mm, F.Cu at (184.5, 91.7)
- moved TP10 1.29 mm to (92.9, 52.7)
- moved TP11 1.29 mm to (94.9, 52.7)
- moved TP9 1.29 mm to (96.9, 52.7)
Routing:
- net /nukes/External_Supply: track 53.0 -> 50.8 mm
- net /MOSI: track 161.4 -> 159.8 mm
- net /SCLK: track 133.6 -> 132.3 mm
- net +3V3: track 183.1 -> 182.2 mm
- net /MISO: track 142.4 -> 141.7 mm
